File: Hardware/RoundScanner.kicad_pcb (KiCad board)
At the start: 2 copper layers, 49.1 x 49.1 mm, 76 parts, among them J1 I2C Debug, J2 I2C, Q1 BSS138DW-7-F, U1 OPA2376xxD, U2 NAU7802SGI, U3 LM285D-2.5, U4 TPS61023DRLR, U5 TLC59208FIPWR, U6 AS7341-DLGT, U7 AP7312-1833W6-7

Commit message: DRC Cleanup
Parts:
- removed the REF** at (100.6, 113.4)
- removed the REF** at (95.2, 91.2)
- removed the REF** at (89.4, 123.3)
- removed the REF** at (72.3, 97.0)
- added J3: I2C, Connector_JST:JST_SH_SM04B-SRSS-TB_1x04-1MP_P1.00mm_Horizontal, B.Cu at (97.5, 121.7)
- added REF**: MountingHole_2.2mm_M2_ISO7380_Pad, MountingHole:MountingHole_2.2mm_M2_ISO7380_Pad, F.Cu at (89.4, 123.6)
- added REF**: MountingHole_2.2mm_M2_ISO7380_Pad, MountingHole:MountingHole_2.2mm_M2_ISO7380_Pad, F.Cu at (72.4, 97.3)
- added REF**: MountingHole_2.2mm_M2_ISO7380_Pad, MountingHole:MountingHole_2.2mm_M2_ISO7380_Pad, F.Cu at (95.9, 91.9)
- added REF**: MountingHole_2.2mm_M2_ISO7380_Pad, MountingHole:MountingHole_2.2mm_M2_ISO7380_Pad, F.Cu at (85.6, 100.8)
- added REF**: MountingHole_2.2mm_M2_ISO7380_Pad, MountingHole:MountingHole_2.2mm_M2_ISO7380_Pad, F.Cu at (101.1, 113.5)
- U7: value AP7312-1833W6-7 -> SOT26_DIO
- moved TP4 0.28 mm to (99.9, 98.9)
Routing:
- net SDA: track 123.1 -> 126.2 mm
- net Net-(C3-Pad2): track 17.9 -> 15.3 mm
- net +3V3: track 179.1 -> 181.5 mm, vias 8 -> 9
- net Net-(R29-Pad1): track 22.4 -> 20.1 mm
- net SCL: track 101.9 -> 103.9 mm
- net +1V8: track 32.1 -> 33.9 mm
- net GND: track 202.0 -> 203.7 mm, vias 9 -> 10
- net Net-(C3-Pad1): track 19.9 -> 18.9 mm
- net +2V5: track 38.0 -> 38.9 mm

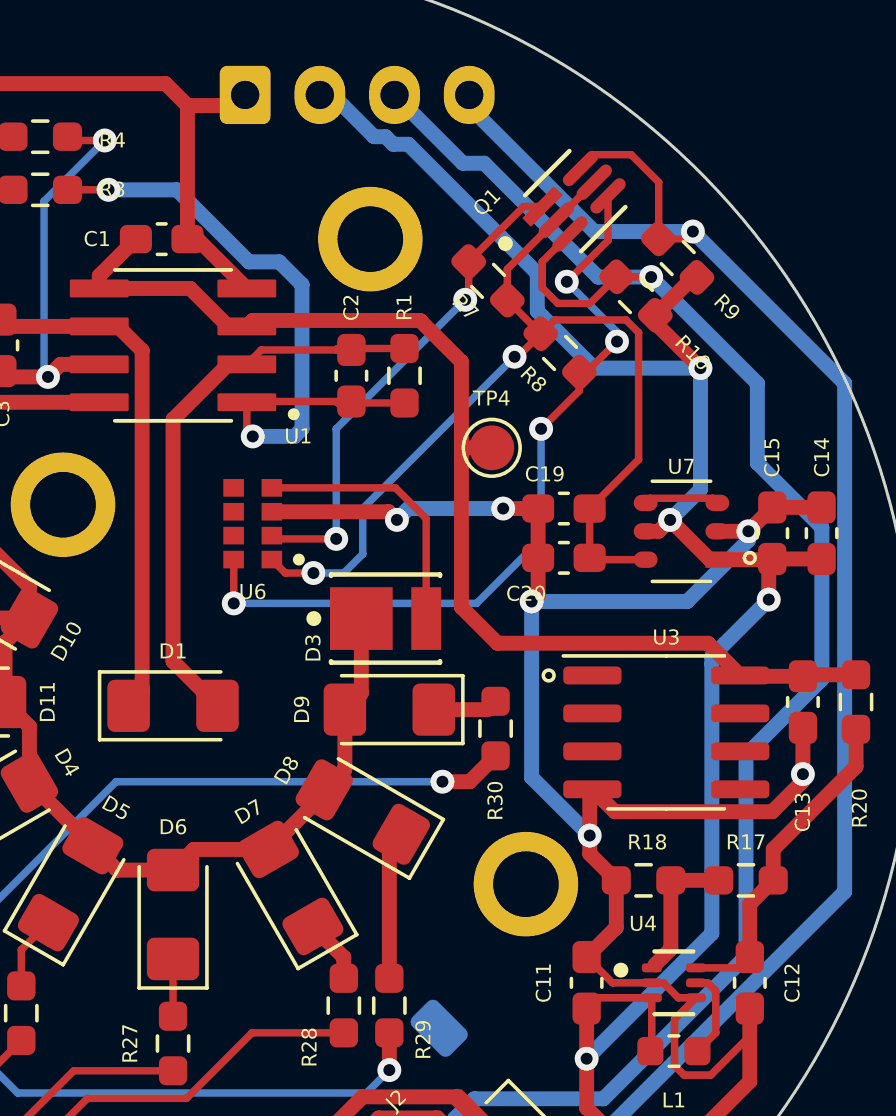
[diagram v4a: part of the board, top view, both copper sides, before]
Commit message: Readme + hole update
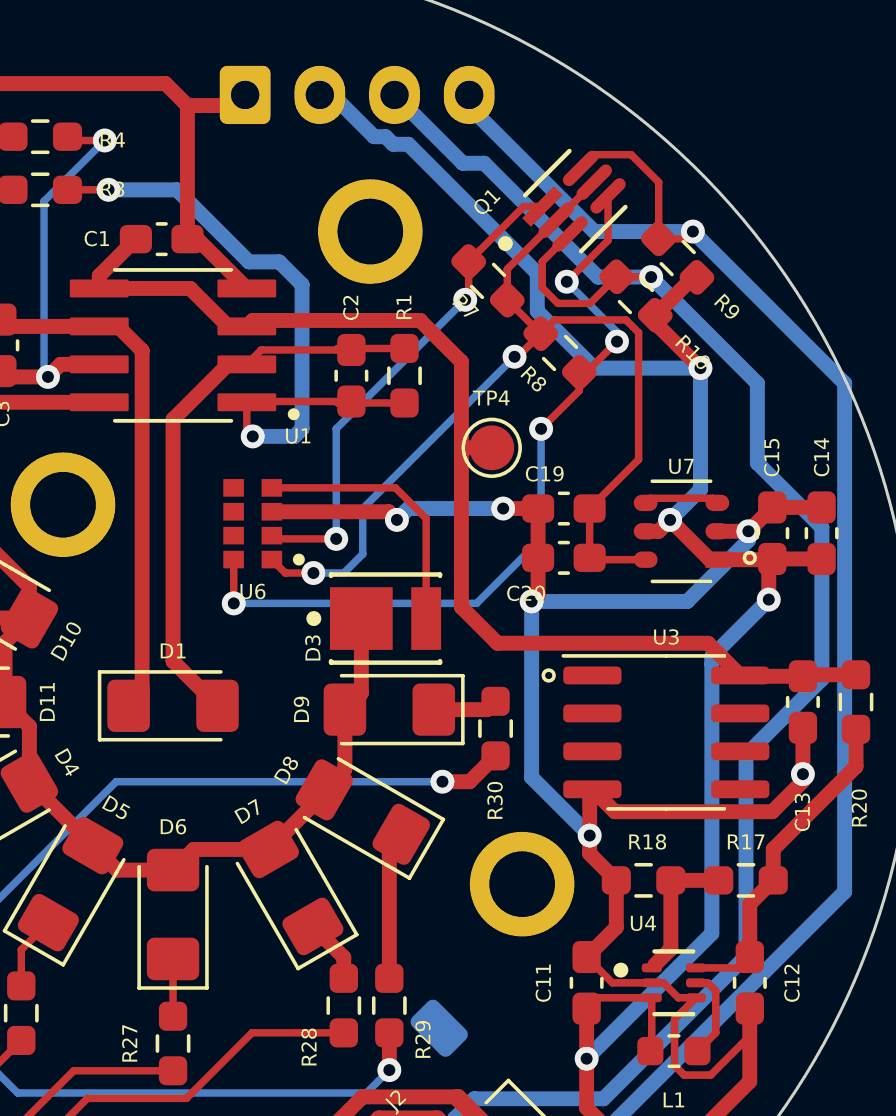
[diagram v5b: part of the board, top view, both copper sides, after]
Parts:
- removed REF** (x5): MountingHole_2.2mm_M2_ISO7380_Pad, MountingHole:MountingHole_2.2mm_M2_ISO7380_Pad
- added H1: MountingHole, MountingHole:MountingHole_2.2mm_M2_ISO7380_Pad, F.Cu at (89.4, 123.6)
- added H2: MountingHole, MountingHole:MountingHole_2.2mm_M2_ISO7380_Pad, F.Cu at (85.6, 100.8)
- added H3: MountingHole, MountingHole:MountingHole_2.2mm_M2_ISO7380_Pad, F.Cu at (101.0, 113.5)
- added H4: MountingHole, MountingHole:MountingHole_2.2mm_M2_ISO7380_Pad, F.Cu at (95.9, 91.7)
- added H5: MountingHole, MountingHole:MountingHole_2.2mm_M2_ISO7380_Pad, F.Cu at (72.4, 97.3)
- U7: value SOT26_DIO -> AP7312-1833W6-7
